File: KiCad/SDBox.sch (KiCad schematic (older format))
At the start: 19 parts, among them J1 DB25_Male, J2 Micro_SD_Card_Socket, U2 SN74CB3T16210

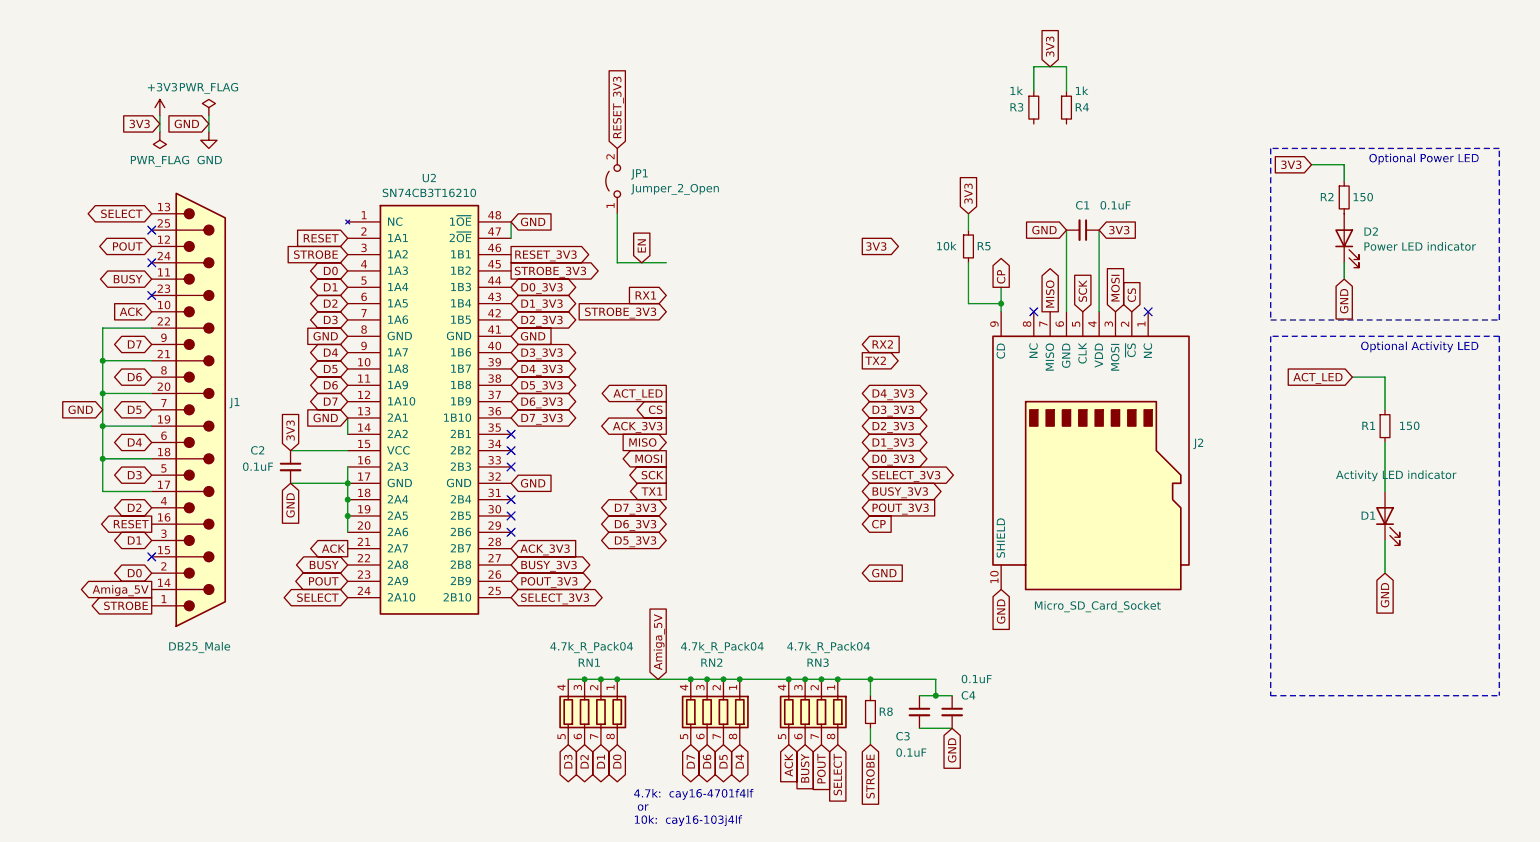
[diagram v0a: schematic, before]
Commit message: Update design to accomodate a Rapberry_Pi_Pico_2W
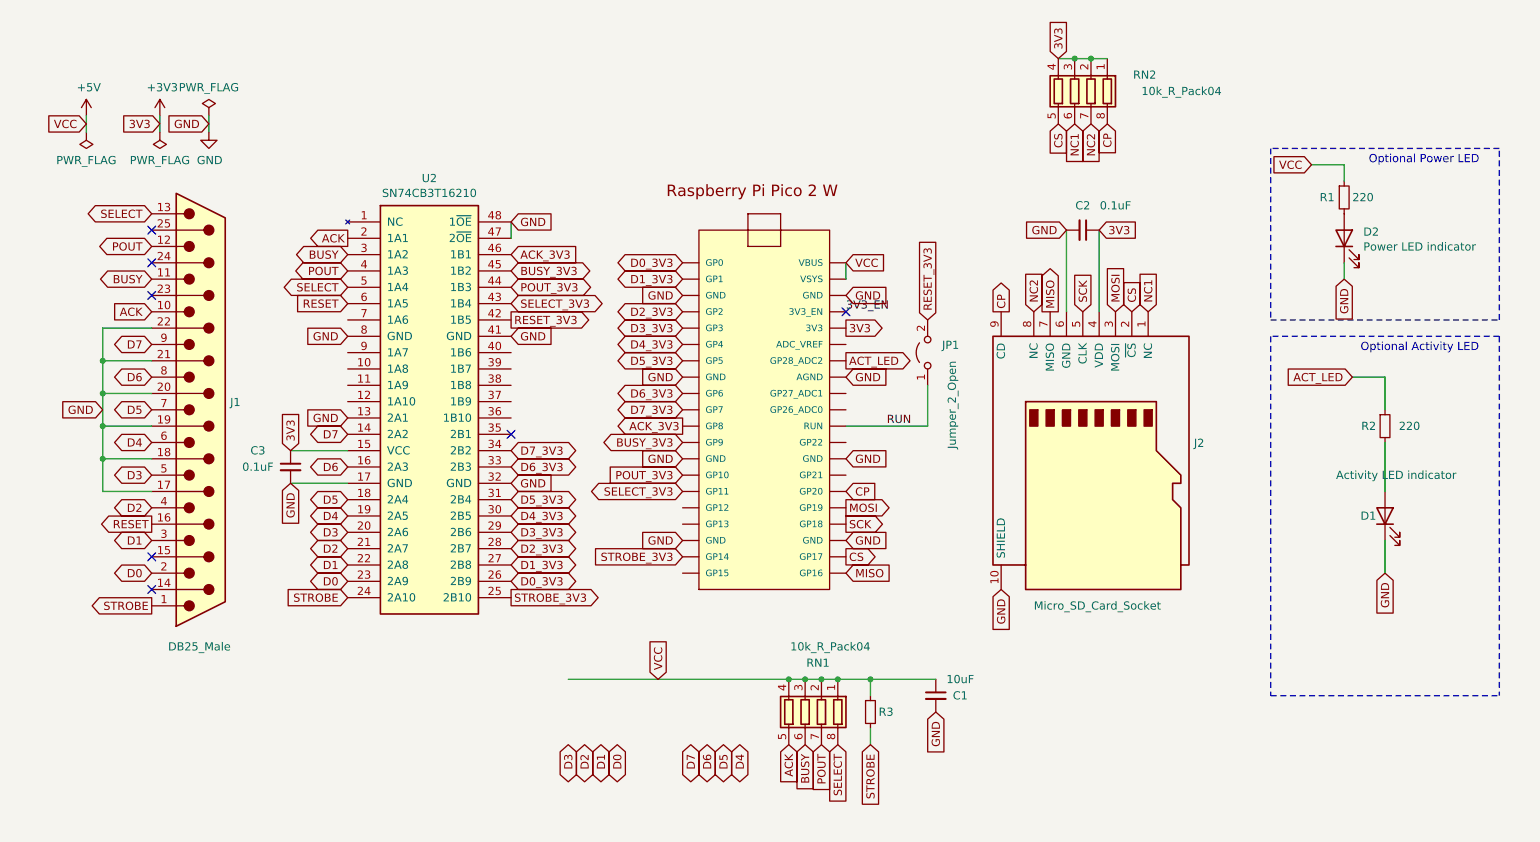
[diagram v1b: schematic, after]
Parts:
- removed C4: 0.1uF, Capacitor_SMD:C_0805_2012Metric_Pad1.15x1.40mm_HandSolder, symbol Device:C_Small
- removed R3, R4: 1k, Resistor_SMD:R_0603_1608Metric_Pad1.05x0.95mm_HandSolder, symbol Device:R_Small
- removed R5: 10k, Resistor_SMD:R_0603_1608Metric_Pad1.05x0.95mm_HandSolder, symbol Device:R_Small
- removed RN1: 4.7k_R_Pack04, Parallel_to_ESP32:RESCAF80P320X160X60-8N, symbol Device:R_Pack04
- added U1: Rapberry_Pi_Pico_2W, SDBox:RPi_Pico_SMD, symbol SDBox:Rapberry_Pi_Pico_2W
- C1: renamed from C3; value 0.1uF -> 10uF; footprint Capacitor_SMD:C_0805_2012Metric_Pad1.15x1.40mm_HandSolder -> Capacitor_SMD:C_1206_3216Metric_Pad1.33x1.80mm_HandSolder
- C3: renamed from C2; footprint Capacitor_SMD:C_0805_2012Metric_Pad1.15x1.40mm_HandSolder -> Capacitor_SMD:C_0603_1608Metric_Pad1.08x0.95mm_HandSolder
- D1, D2: footprint LED_THT:LED_D3.0mm -> LED_THT:LED_Rectangular_W5.0mm_H2.0mm
- R1: renamed from R2; value 150 -> 220
- R2: renamed from R1; value 150 -> 220
- RN1: renamed from RN3; value 4.7k_R_Pack04 -> 10k_R_Pack04; footprint Parallel_to_ESP32:RESCAF80P320X160X60-8N -> SDBox:RESCAF80P320X160X60-8N
- RN2: value 4.7k_R_Pack04 -> 10k_R_Pack04; footprint Parallel_to_ESP32:RESCAF80P320X160X60-8N -> SDBox:RESCAF80P320X160X60-8N
- renumbered C1 to C2, R8 to R3
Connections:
- net +3V3: now also RN2.1 (R1.1), RN2.2 (R2.1), RN2.3 (R3.1), RN2.4 (R4.1), U1.36 (3V3); no longer R1.1
- net ACK: now also U2.2 (1A1); no longer U2.21 (2A7)
- net ACK_3V3: now also U2.46 (1B1), U1.11 (GP8); no longer U2.28 (2B7)
- net ACT_LED: now also U1.34 (GP28_ADC2)
- net BUSY: now also U2.3 (1A2); no longer U2.22 (2A8)
- net BUSY_3V3: now also U2.45 (1B2), U1.12 (GP9); no longer U2.27 (2B8)
- net CP: now also RN2.8 (R1.2), U1.26 (GP20)
- net CS: now also RN2.5 (R4.2), U1.22 (GP17)
- net D0: now also U2.23 (2A9); no longer U2.4 (1A3)
- net D0_3V3: now also U2.26 (2B9), U1.1 (GP0); no longer U2.44 (1B3)
- net D1: now also U2.22 (2A8); no longer U2.5 (1A4)
- net D1_3V3: now also U2.27 (2B8), U1.2 (GP1); no longer U2.43 (1B4)
- net D2: now also U2.21 (2A7); no longer U2.6 (1A5)
- net D2_3V3: now also U2.28 (2B7), U1.4 (GP2); no longer U2.42 (1B5)
- net D3: now also U2.20 (2A6); no longer U2.7 (1A6)
- net D3_3V3: now also U2.29 (2B6), U1.5 (GP3); no longer U2.40 (1B6)
- net D4: now also U2.19 (2A5); no longer RN2.8 (R1.2), U2.9 (1A7)
- net D4_3V3: now also U2.30 (2B5), U1.6 (GP4); no longer U2.39 (1B7)
- net D5: now also U2.18 (2A4); no longer RN2.7 (R2.2), U2.10 (1A8)
- net D5_3V3: now also U2.31 (2B4), U1.7 (GP5); no longer U2.38 (1B8)
- net D6: now also U2.16 (2A3); no longer RN2.6 (R3.2), U2.11 (1A9)
- net D6_3V3: now also U2.33 (2B3), U1.9 (GP6); no longer U2.37 (1B9)
- net D7: now also U2.14 (2A2); no longer RN2.5 (R4.2), U2.12 (1A10)
- net D7_3V3: now also U2.34 (2B2), U1.10 (GP7); no longer U2.36 (1B10)
- net GND: now also U1.13 (GND), U1.18 (GND), U1.23 (GND), U1.28 (GND), U1.3 (GND), U1.33 (AGND), U1.38 (GND), U1.8 (GND); no longer U2.14 (2A2), U2.16 (2A3), U2.18 (2A4), U2.19 (2A5), U2.20 (2A6)
- net MISO: now also U1.21 (GP16)
- net MOSI: now also U1.25 (GP19)
- net POUT: now also U2.4 (1A3); no longer U2.23 (2A9)
- net POUT_3V3: now also U2.44 (1B3), U1.14 (GP10); no longer U2.26 (2B9)
- net RESET: now also U2.6 (1A5); no longer U2.2 (1A1)
- net RESET_3V3: now also U2.42 (1B5); no longer U2.46 (1B1)
- net SCK: now also U1.24 (GP18)
- net SELECT: now also U2.5 (1A4); no longer U2.24 (2A10)
- net SELECT_3V3: now also U2.43 (1B4), U1.15 (GP11); no longer U2.25 (2B10)
- net STROBE: now also U2.24 (2A10); no longer U2.3 (1A2)
- net STROBE_3V3: now also U2.25 (2B10), U1.19 (GP14); no longer U2.45 (1B2)
- net NC1: now reaches J2.1 (NC)
- net NC1: now also RN2.6 (R3.2)
- net NC2: now reaches J2.8 (NC)
- net NC2: now also RN2.7 (R2.2)
- net Amiga_5V renamed +5V
- net +5V: now also R1.1, U1.39 (VSYS), U1.40 (VBUS); no longer J1.14 (P14), RN2.1 (R1.1), RN2.2 (R2.1), RN2.3 (R3.1), RN2.4 (R4.1)
- net EN renamed RUN
- net RUN: now also U1.30 (RUN)
- new net 3V3_EN: U1.37 (3V3_EN)
- no-connect marks 12 -> 7
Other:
- note removed: "4.7k: cay16-4701f4lf\n or\n10k: cay16-103j4lf"
- moved on the sheet: C1, JP1

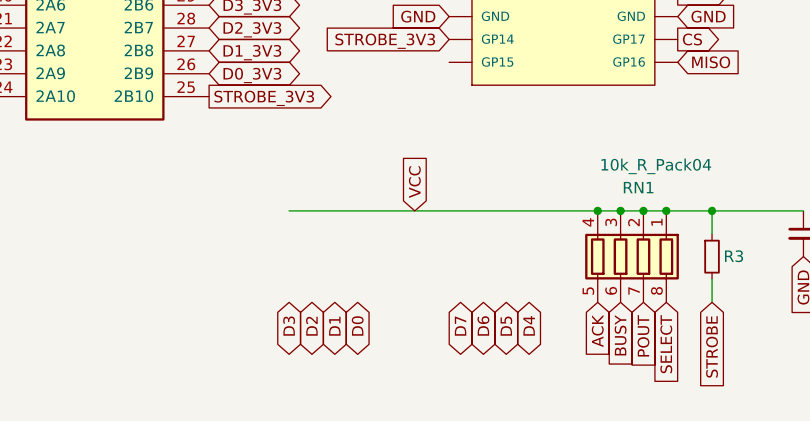
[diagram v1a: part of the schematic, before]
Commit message: Add RN3 (pull-ups for data lines), fixed keep-out areas for header and test-points on RPi Pico 2 W
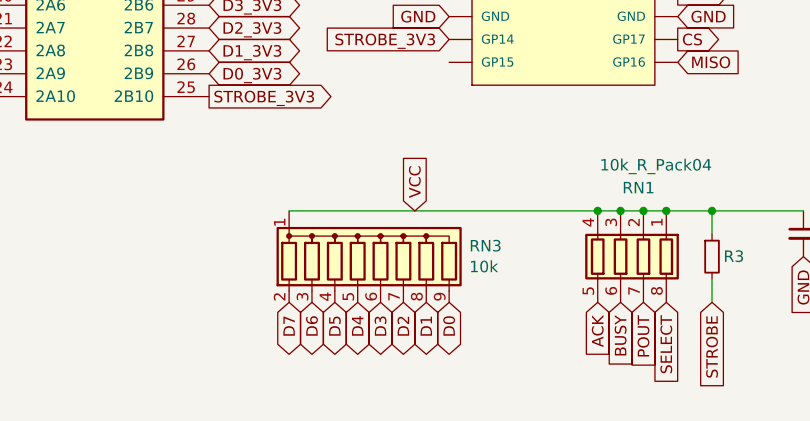
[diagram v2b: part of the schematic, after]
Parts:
- added RN3: 10k, Resistor_THT:R_Array_SIP9, symbol Device:R_Network08
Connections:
- net +5V: now also RN3.1 (common)
- net D0: now also RN3.9 (R8)
- net D1: now also RN3.8 (R7)
- net D2: now also RN3.7 (R6)
- net D3: now also RN3.6 (R5)
- net D4: now also RN3.5 (R4)
- net D5: now also RN3.4 (R3)
- net D6: now also RN3.3 (R2)
- net D7: now also RN3.2 (R1)
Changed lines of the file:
@@
 Wire Wire Line
 	5550 5850 5650 5850
-Text GLabel 4400 6250 3    50   BiDi ~ 0
+Text GLabel 4800 6250 3    50   BiDi ~ 0
 D0
-Text GLabel 4300 6250 3    50   BiDi ~ 0
+Text GLabel 4700 6250 3    50   BiDi ~ 0
 D1
-Text GLabel 4200 6250 3    50   BiDi ~ 0
+Text GLabel 4600 6250 3    50   BiDi ~ 0
 D2
-Text GLabel 4100 6250 3    50   BiDi ~ 0
+Text GLabel 4500 6250 3    50   BiDi ~ 0
 D3
 Text GLabel 5950 6250 3    50   Input ~ 0
 STROBE
-Text GLabel 4950 6250 3    50   BiDi ~ 0
+Text GLabel 4200 6250 3    50   BiDi ~ 0
 D6
-Text GLabel 4850 6250 3    50   BiDi ~ 0
+Text GLabel 4100 6250 3    50   BiDi ~ 0
 D7
-Text GLabel 5150 6250 3    50   BiDi ~ 0
+Text GLabel 4400 6250 3    50   BiDi ~ 0
 D4
-Text GLabel 5050 6250 3    50   BiDi ~ 0
+Text GLabel 4300 6250 3    50   BiDi ~ 0
 D5
 $Comp
@@
 Wire Wire Line
 	4100 5850 5450 5850
+$Comp
+L Device:R_Network08 RN3
+U 1 1 684FD3D5
+P 4500 6050
+F 0 "RN3" H 4888 6096 50  0000 L CNN
+F 1 "10k" H 4888 6005 50  0000 L CNN
+F 2 "Resistor_THT:R_Array_SIP9" V 4975 6050 50  0001 C CNN
+F 3 "http://www.vishay.com/docs/31509/csc.pdf" H 4500 6050 50  0001 C CNN
+	1    4500 6050
+	1    0    0    -1
+$EndComp
 $EndSCHEMATC

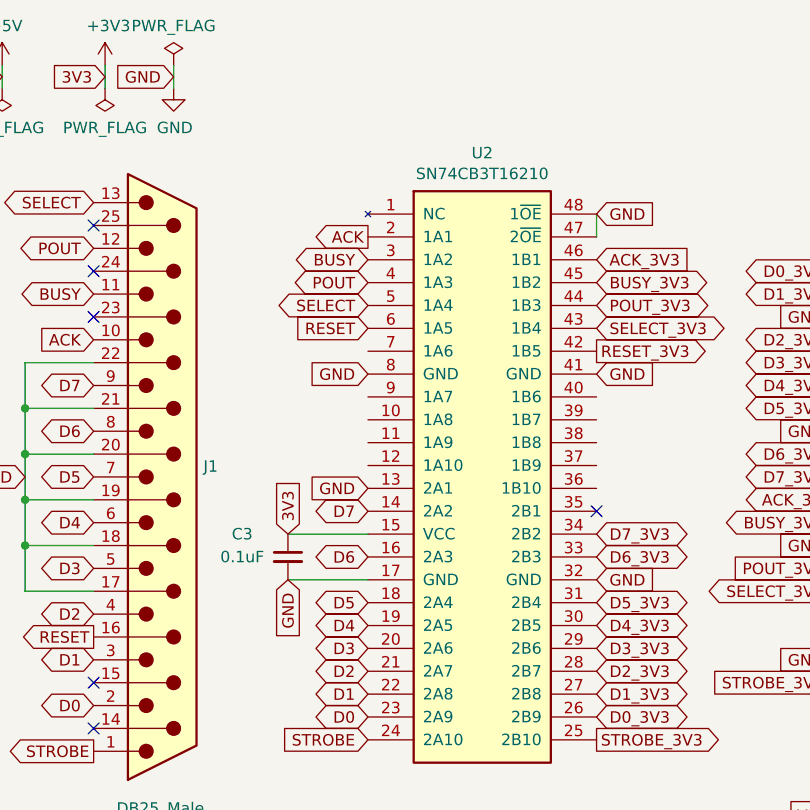
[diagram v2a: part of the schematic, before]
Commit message: Change U2 SN74CB3T16210 to SN74CBT16210 and add diode D3 and resistor R4 to drop VCC to 4.3V power supply for U2
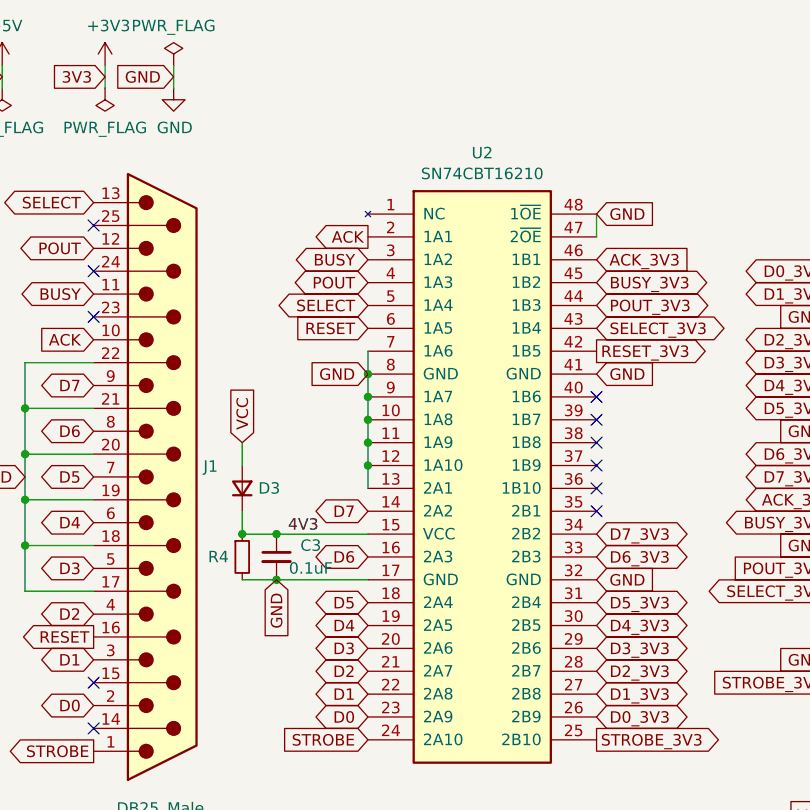
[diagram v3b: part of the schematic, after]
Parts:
- removed U2: SN74CB3T16210, Package_SO:TSSOP-48_6.1x12.5mm_P0.5mm, symbol SDBox:SN74CB3T16210
- added D3: D_Small, Diode_SMD:D_0603_1608Metric_Pad1.05x0.95mm_HandSolder, symbol Device:D_Small
- added R4: 2.9k, Resistor_SMD:R_0603_1608Metric_Pad0.98x0.95mm_HandSolder, symbol Device:R_Small
- added U2: SN74CBT16210, Package_SO:TSSOP-48_6.1x12.5mm_P0.5mm, symbol SDBox:SN74CBT16210
- R3: footprint Resistor_SMD:R_0603_1608Metric_Pad1.05x0.95mm_HandSolder -> Resistor_SMD:R_0603_1608Metric_Pad0.98x0.95mm_HandSolder
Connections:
- net +3V3: no longer C3.1
- net +5V: now also D3.2 (A)
- net ACK: now also U2.2 (1A1)
- net ACK_3V3: now also U2.46 (1B1)
- net BUSY: now also U2.3 (1A2)
- net BUSY_3V3: now also U2.45 (1B2)
- net D0: now also U2.23 (2A9)
- net D0_3V3: now also U2.26 (2B9)
- net D1: now also U2.22 (2A8)
- net D1_3V3: now also U2.27 (2B8)
- net D2: now also U2.21 (2A7)
- net D2_3V3: now also U2.28 (2B7)
- net D3: now also U2.20 (2A6)
- net D3_3V3: now also U2.29 (2B6)
- net D4: now also U2.19 (2A5)
- net D4_3V3: now also U2.30 (2B5)
- net D5: now also U2.18 (2A4)
- net D5_3V3: now also U2.31 (2B4)
- net D6: now also U2.16 (2A3)
- net D6_3V3: now also U2.33 (2B3)
- net D7: now also U2.14 (2A2)
- net D7_3V3: now also U2.34 (2B2)
- net GND: now also R4.2, U2.10 (1A8), U2.11 (1A9), U2.12 (1A10), U2.13 (2A1), U2.17 (GND), U2.32 (GND), U2.41 (GND), U2.47 (2~OE), U2.48 (1~OE), U2.7 (1A6), U2.8 (GND), U2.9 (1A7)
- net POUT: now also U2.4 (1A3)
- net POUT_3V3: now also U2.44 (1B3)
- net RESET: now also U2.6 (1A5)
- net RESET_3V3: now also U2.42 (1B5)
- net SELECT: now also U2.5 (1A4)
- net SELECT_3V3: now also U2.43 (1B4)
- net STROBE: now also U2.24 (2A10)
- net STROBE_3V3: now also U2.25 (2B10)
- new net 4V3: C3.1, D3.1 (K), R4.1, U2.15 (VCC)
- no-connect marks 7 -> 12
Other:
- moved on the sheet: C3
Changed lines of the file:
@@
 Text GLabel 2750 3750 0    50   Input ~ 0
 GND
-Text GLabel 2400 4650 3    50   Input ~ 0
+Text GLabel 2350 4650 3    50   Input ~ 0
 GND
 Text GLabel 3750 4650 2    50   Input ~ 0
@@
 Text GLabel 3750 3750 2    50   Input ~ 0
 GND
-Text GLabel 2400 4450 1    50   Input ~ 0
-3V3
-$Comp
-L SDBox:SN74CB3T16210 U2
-U 1 1 6442C4B2
-P 3250 4150
-F 0 "U2" H 3250 5517 50  0000 C CNN
-F 1 "SN74CB3T16210" H 3250 5426 50  0000 C CNN
-F 2 "Package_SO:TSSOP-48_6.1x12.5mm_P0.5mm" H 4900 4600 50  0001 C CNN
-F 3 "https://www.ti.com/lit/ds/symlink/sn74cb3t16210.pdf" H 4900 4600 50  0001 C CNN
-	1    3250 4150
-	1    0    0    -1
-$EndComp
 $Comp
 L power:+3V3 #PWR0101
@@
 Text GLabel 3750 4450 2    50   BiDi ~ 0
 D7_3V3
-Text GLabel 2750 4250 0    50   Input ~ 0
-GND
 NoConn ~ 3750 4350
 Text GLabel 1550 5400 0    50   Output ~ 0
@@
 L Device:C_Small C3
 U 1 1 6448FFBE
-P 2400 4550
-F 0 "C3" H 2200 4650 50  0000 C CNN
-F 1 "0.1uF" H 2200 4550 50  0000 C CNN
-F 2 "Capacitor_SMD:C_0603_1608Metric_Pad1.08x0.95mm_HandSolder" H 2400 4550 50  0001 C CNN
-F 3 "~" H 2400 4550 50  0001 C CNN
-	1    2400 4550
-	1    0    0    -1
-$EndComp
-Wire Wire Line
-	2400 4450 2750 4450
-Wire Wire Line
-	2400 4650 2750 4650
+P 2350 4550
+F 0 "C3" H 2500 4600 50  0000 C CNN
+F 1 "0.1uF" H 2500 4500 50  0000 C CNN
+F 2 "Capacitor_SMD:C_0603_1608Metric_Pad1.08x0.95mm_HandSolder" H 2350 4550 50  0001 C CNN
+F 3 "~" H 2350 4550 50  0001 C CNN
+	1    2350 4550
+	1    0    0    -1
+$EndComp
 Wire Wire Line
 	3750 3150 3750 3050
@@
 F 0 "R3" H 6000 6050 50  0000 L CNN
 F 1 "10k" H 5750 6050 50  0001 L CNN
-F 2 "Resistor_SMD:R_0603_1608Metric_Pad1.05x0.95mm_HandSolder" H 5950 6050 50  0001 C CNN
+F 2 "Resistor_SMD:R_0603_1608Metric_Pad0.98x0.95mm_HandSolder" H 5950 6050 50  0001 C CNN
 F 3 "~" H 5950 6050 50  0001 C CNN
 	1    5950 6050
@@
 	1    0    0    -1
 $EndComp
+$Comp
+L SDBox:SN74CBT16210 U2
+U 1 1 6850D73F
+P 3250 4150
+F 0 "U2" H 3250 5517 50  0000 C CNN
+F 1 "SN74CBT16210" H 3250 5426 50  0000 C CNN
+F 2 "Package_SO:TSSOP-48_6.1x12.5mm_P0.5mm" H 4900 4600 50  0001 C CNN
+F 3 "" H 4900 4600 50  0001 C CNN
+	1    3250 4150
+	1    0    0    -1
+$EndComp
+Wire Wire Line
+	2750 3650 2750 3750
+Wire Wire Line
+	2750 3750 2750 3850
+Connection ~ 2750 3750
+Connection ~ 2750 3850
+Wire Wire Line
+	2750 3850 2750 3950
+Connection ~ 2750 3950
+Wire Wire Line
+	2750 3950 2750 4050
+Connection ~ 2750 4050
+Wire Wire Line
+	2750 4050 2750 4150
+Connection ~ 2750 4150
+Wire Wire Line
+	2750 4150 2750 4250
+NoConn ~ 3750 4250
+NoConn ~ 3750 4150
+NoConn ~ 3750 4050
+NoConn ~ 3750 3950
+NoConn ~ 3750 3850
+$Comp
+L Device:D_Small D3
+U 1 1 6852D7AF
+P 2200 4250
+F 0 "D3" V 2200 4180 50  0000 R CNN
+F 1 "D_Small" V 2155 4180 50  0001 R CNN
+F 2 "Diode_SMD:D_0603_1608Metric_Pad1.05x0.95mm_HandSolder" V 2200 4250 50  0001 C CNN
+F 3 "~" V 2200 4250 50  0001 C CNN
+	1    2200 4250
+	0    -1   -1   0
+$EndComp
+Text GLabel 2200 4050 1    50   Input ~ 0
+VCC
+Wire Wire Line
+	2350 4650 2750 4650
+Wire Wire Line
+	2350 4450 2750 4450
+$Comp
+L Device:R_Small R4
+U 1 1 685336A8
+P 2200 4550
+F 0 "R4" H 2050 4550 50  0000 L CNN
+F 1 "2.9k" H 2000 4550 50  0001 L CNN
+F 2 "Resistor_SMD:R_0603_1608Metric_Pad0.98x0.95mm_HandSolder" H 2200 4550 50  0001 C CNN
+F 3 "~" H 2200 4550 50  0001 C CNN
+	1    2200 4550
+	1    0    0    -1
+$EndComp
+Wire Wire Line
+	2200 4050 2200 4150
+Wire Wire Line
+	2200 4350 2200 4450
+Wire Wire Line
+	2200 4450 2350 4450
+Connection ~ 2200 4450
+Connection ~ 2350 4450
+Wire Wire Line
+	2350 4650 2200 4650
+Connection ~ 2350 4650
+Text Label 2400 4450 0    50   ~ 0
+4V3
 $EndSCHEMATC
